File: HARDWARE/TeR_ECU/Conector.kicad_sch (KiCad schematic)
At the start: 1 part, among them IC1 MX34040NF2

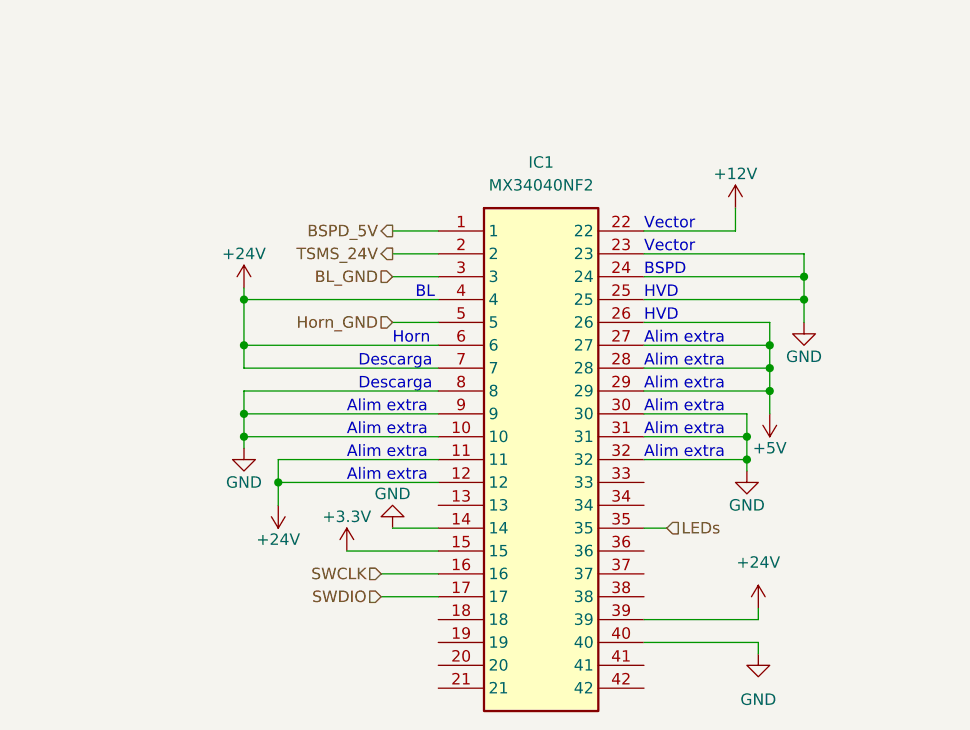
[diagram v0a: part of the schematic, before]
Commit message: Falata routear señales al conector
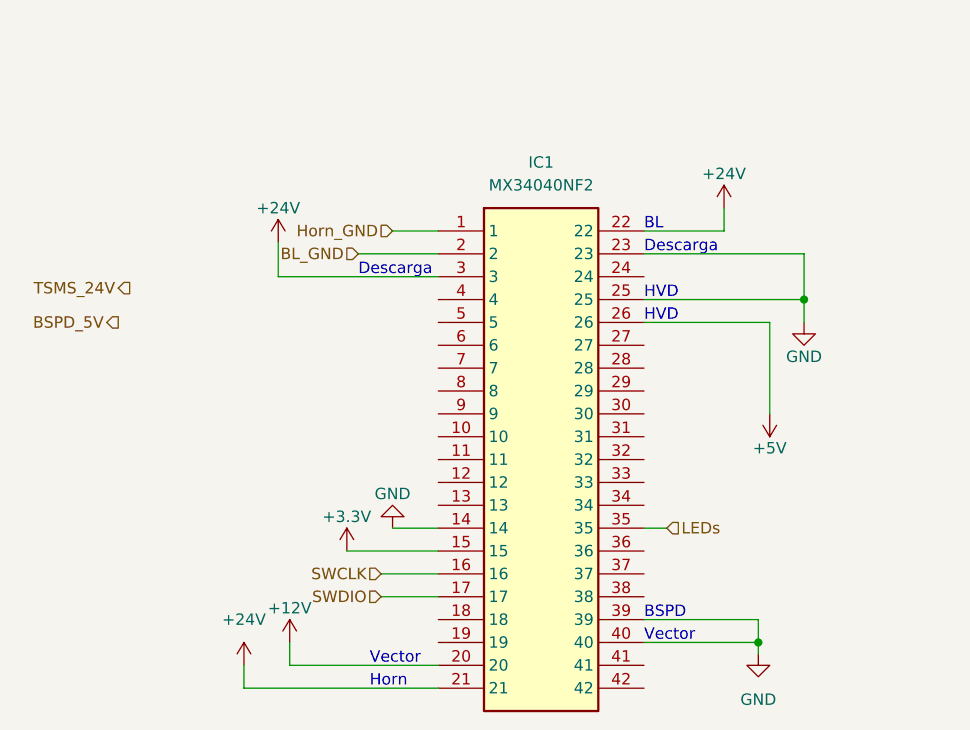
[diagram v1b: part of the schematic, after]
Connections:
- net +12V: now also IC1.20; no longer IC1.22
- net +24V: now also IC1.21, IC1.22, IC1.3; no longer IC1.11, IC1.12, IC1.39, IC1.4, IC1.6, IC1.7
- net +5V: no longer IC1.27, IC1.28, IC1.29
- net BL_GND: now also IC1.2; no longer IC1.3
- net BSPD_5V: no longer IC1.1
- net GND: now also IC1.39; no longer IC1.10, IC1.24, IC1.30, IC1.31, IC1.32, IC1.8, IC1.9
- net Horn_GND: now also IC1.1; no longer IC1.5
- net TSMS_24V: no longer IC1.2
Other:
- note removed: "Alim extra"

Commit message: Solo falta revisar
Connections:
- net +24V: now also IC1.8, IC1.9
- net +3.3V: now also IC1.5; no longer IC1.15
- net +5V: now also IC1.13, IC1.14, IC1.15, IC1.19, IC1.27; no longer IC1.26
- net BSPD_5V: now also IC1.17
- net GND: now also IC1.26, IC1.28, IC1.29, IC1.35, IC1.36, IC1.37, IC1.38; no longer IC1.14
- net LEDs: now also IC1.18; no longer IC1.35
- net SWCLK: now also IC1.4; no longer IC1.16
- net SWDIO: now also IC1.24; no longer IC1.17
- net TSMS_24V: now also IC1.16
- net UART_RX: now reaches IC1.6
- net UART_TX: now reaches IC1.7
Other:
- note added: "Extra 24V"
- note added: "Extra 5V"
- note added: "IMU"

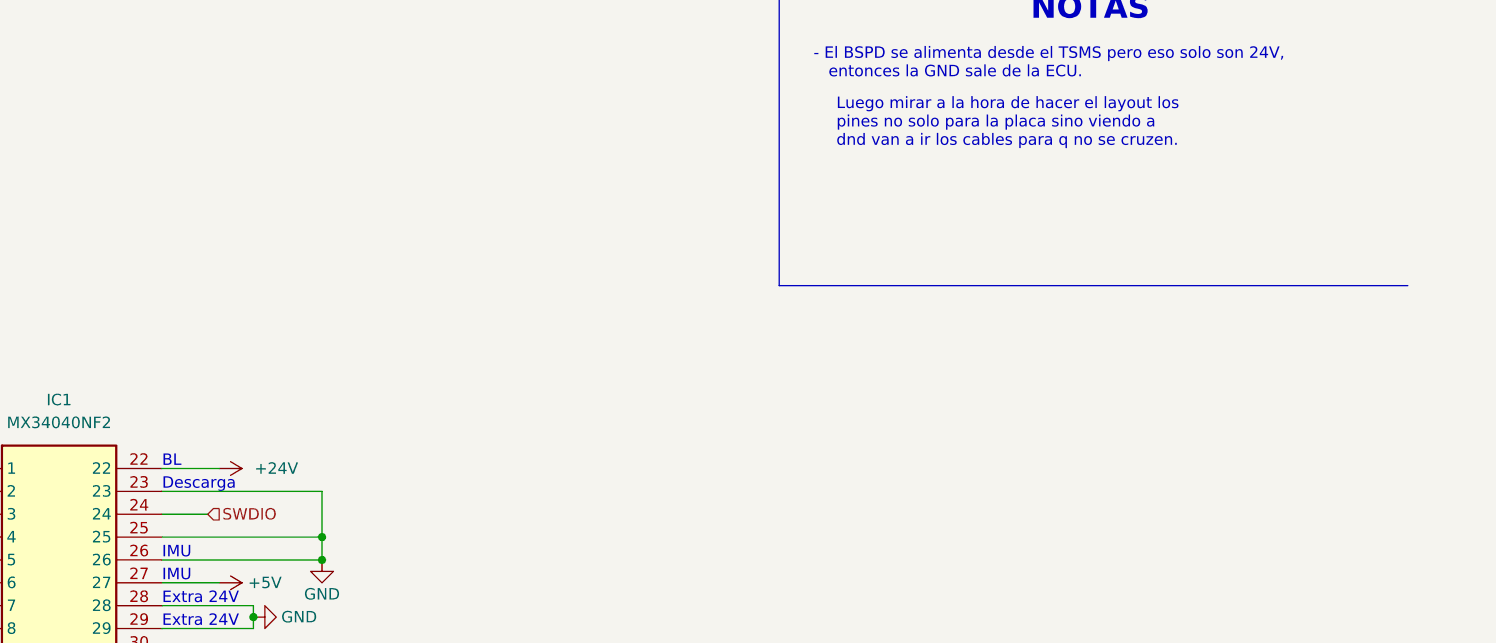
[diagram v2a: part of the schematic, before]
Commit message: Añadida resistencia luz de freno
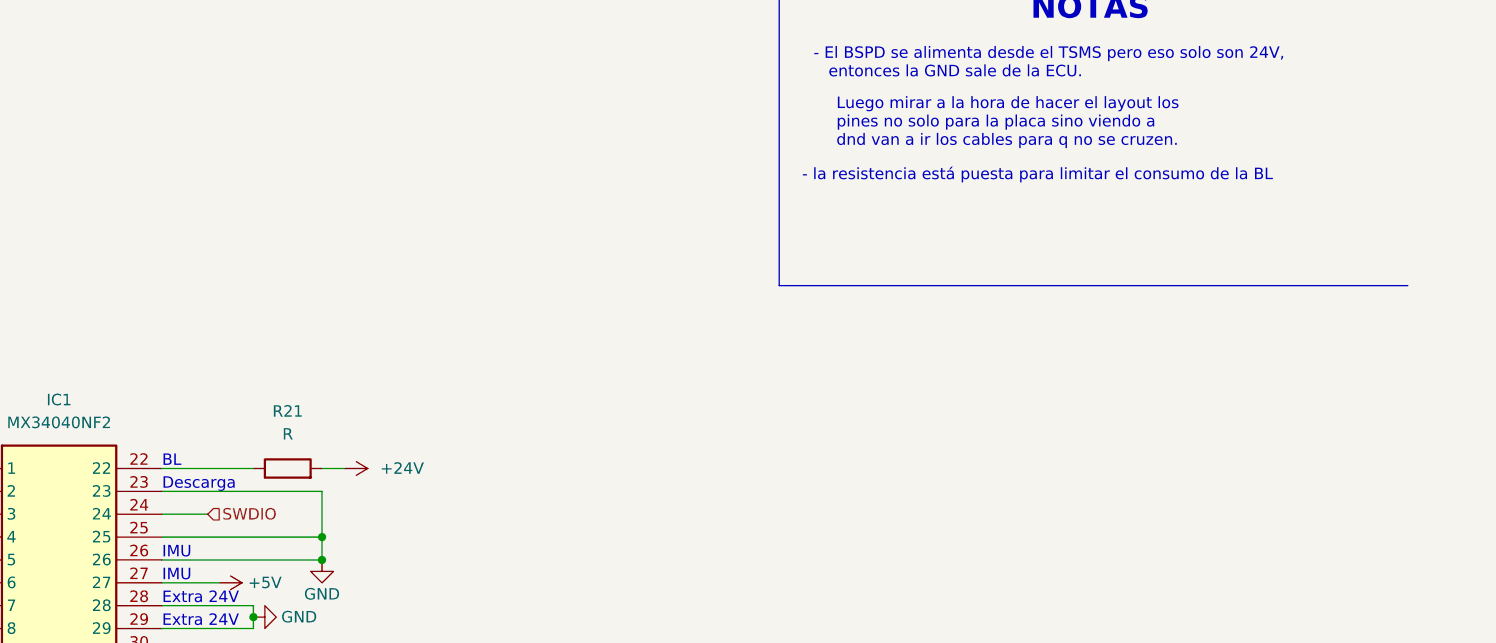
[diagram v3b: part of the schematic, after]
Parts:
- added R21: R, Resistor_SMD:R_0805_2012Metric, symbol Device:R
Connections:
- net +24V: now also R21.2; no longer IC1.22
- new net: IC1.22, R21.1
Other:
- note added: "- la resistencia está puesta para limitar el consumo de la BL"
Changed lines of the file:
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@@
     (stroke (width 0) (type default))
   )
-  (wire (pts (xy 147.32 68.58) (xy 153.67 68.58))
+  (wire (pts (xy 147.32 68.58) (xy 157.48 68.58))
     (stroke (width 0) (type default))
   )
@@
     (stroke (width 0) (type default))
   )
+  (wire (pts (xy 165.1 68.58) (xy 167.64 68.58))
+    (stroke (width 0) (type default))
+  )
   (wire (pts (xy 147.32 111.76) (xy 160.02 111.76))
     (stroke (width 0) (type default))
@@
   )
   (text "Descarga" (at 115.57 73.66 0)
+    (effects (font (size 1.27 1.27)) (justify left bottom))
+  )
+  (text "- la resistencia está puesta para limitar el consumo de la BL"
+    (at 218.44 36.83 0)
     (effects (font (size 1.27 1.27)) (justify left bottom))
   )
@@
         (path "/84413845-c4f3-4743-bcd2-a67649c90902/e25d0f8a-65a3-47e2-987f-518da8891580"
           (reference "#PWR065") (unit 1)
+        )
+      )
+    )
+  )
+  (symbol (lib_id "Device:R") (at 161.29 68.58 90) (unit 1)
+    (in_bom yes) (on_board yes) (dnp no) (fields_autoplaced)
+    (property "Reference" "R21" (at 161.29 62.23 90)
+      (effects (font (size 1.27 1.27)))
+    )
+    (property "Value" "R" (at 161.29 64.77 90)
+      (effects (font (size 1.27 1.27)))
+    )
+    (property "Footprint" "Resistor_SMD:R_0805_2012Metric" (at 161.29 70.358 90)
+      (effects (font (size 1.27 1.27)) hide)
+    )
+    (property "Datasheet" "~" (at 161.29 68.58 0)
+      (effects (font (size 1.27 1.27)) hide)
+    )
+    (pin "1")
+    (pin "2")
+    (instances
+      (project "TeR_ECU"
+        (path "/84413845-c4f3-4743-bcd2-a67649c90902/e25d0f8a-65a3-47e2-987f-518da8891580"
+          (reference "R21") (unit 1)
         )
       )
@@
     )
   )
-  (symbol (lib_id "power:+24V") (at 153.67 68.58 270) (unit 1)
-    (in_bom yes) (on_board yes) (dnp no)
-    (property "Reference" "#PWR067" (at 149.86 68.58 0)
-      (effects (font (size 1.27 1.27)) hide)
-    )
-    (property "Value" "+24V" (at 160.02 68.58 90)
-      (effects (font (size 1.27 1.27)))
-    )
-    (property "Footprint" "" (at 153.67 68.58 0)
-      (effects (font (size 1.27 1.27)) hide)
-    )
-    (property "Datasheet" "" (at 153.67 68.58 0)
-      (effects (font (size 1.27 1.27)) hide)
-    )
+  (symbol (lib_id "power:+24V") (at 167.64 68.58 270) (unit 1)
+    (in_bom yes) (on_board yes) (dnp no)
+    (property "Reference" "#PWR067" (at 163.83 68.58 0)
+      (effects (font (size 1.27 1.27)) hide)
+    )
+    (property "Value" "+24V" (at 173.99 68.58 90)
+      (effects (font (size 1.27 1.27)))
+    )
+    (property "Footprint" "" (at 167.64 68.58 0)
+      (effects (font (size 1.27 1.27)) hide)
+    )
+    (property "Datasheet" "" (at 167.64 68.58 0)
+      (effects (font (size 1.27 1.27)) hide)
+    )

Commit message: Rethought layout and footprints and fixed fuse normative problem
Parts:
- IC1: footprint MX34040NF2 -> MX34040NF2:MX34040NF2

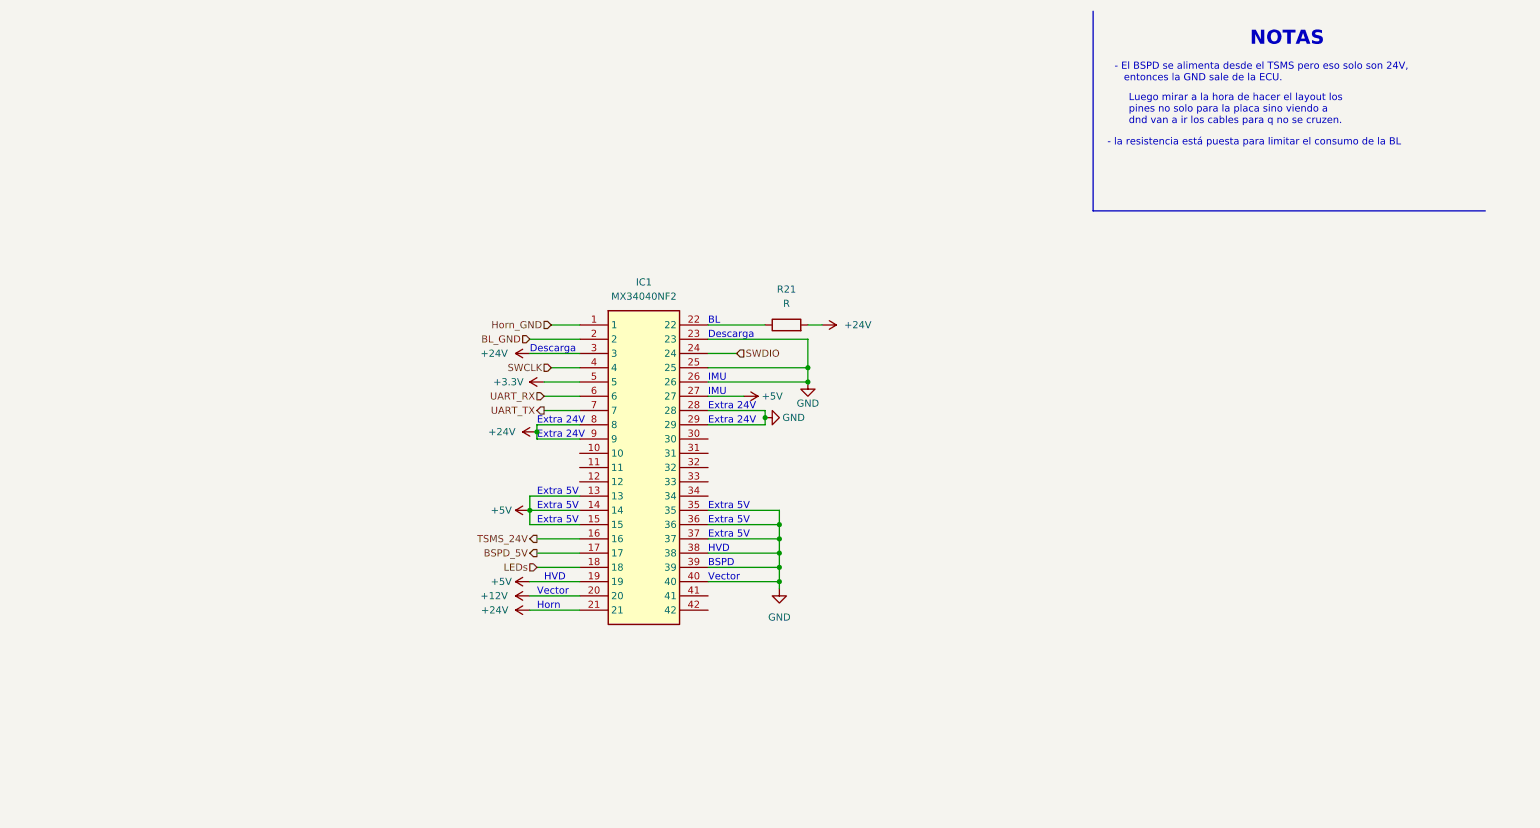
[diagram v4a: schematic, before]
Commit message: Layout V2, added 7-segment display, optimal placement of pins + rework of the boot headers(just one needed)
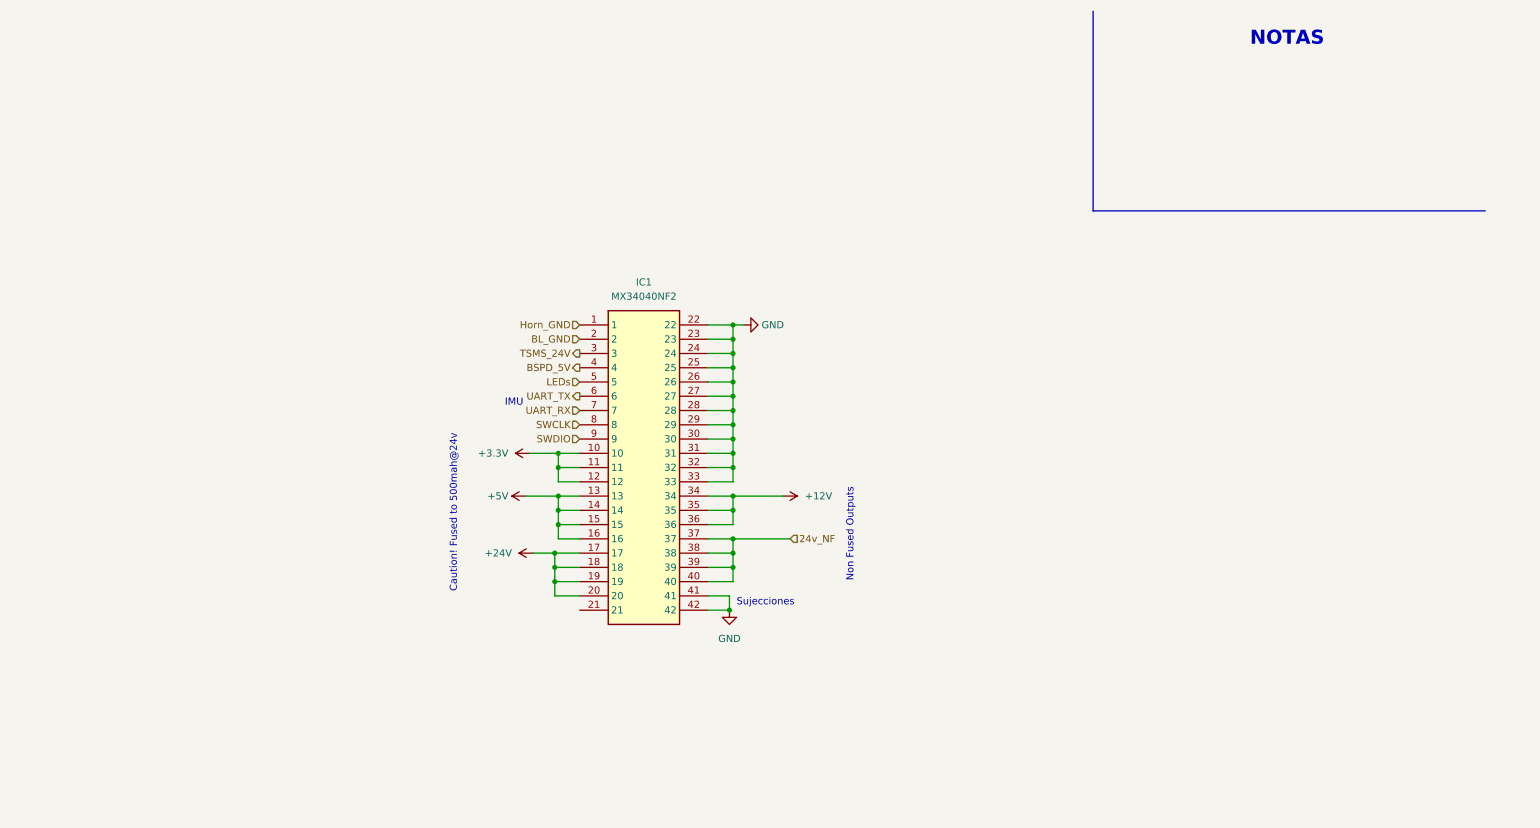
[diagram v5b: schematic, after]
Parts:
- removed R21: R, Resistor_SMD:R_0805_2012Metric, symbol Device:R
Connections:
- net +12V: now also IC1.34, IC1.35, IC1.36; no longer IC1.20
- net +24V: now also IC1.17, IC1.18, IC1.19, IC1.20; no longer IC1.21, IC1.3, IC1.8, IC1.9
- net +3.3V: now also IC1.10, IC1.11, IC1.12; no longer IC1.5
- net +5V: now also IC1.16; no longer IC1.19, IC1.27
- net BSPD_5V: now also IC1.4; no longer IC1.17
- net GND: now also IC1.22, IC1.24, IC1.27, IC1.30, IC1.31, IC1.32, IC1.33, IC1.41, IC1.42; no longer IC1.35, IC1.36, IC1.37, IC1.38, IC1.39, IC1.40
- net LEDs: now also IC1.5; no longer IC1.18
- net SWCLK: now also IC1.8; no longer IC1.4
- net SWDIO: now also IC1.9; no longer IC1.24
- net TSMS_24V: now also IC1.3; no longer IC1.16
- net UART_RX: now also IC1.7; no longer IC1.6
- net UART_TX: now also IC1.6; no longer IC1.7
- new net 24v_NF: IC1.37, IC1.38, IC1.39, IC1.40
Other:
- note added: "Caution! Fused to 500mah@24v"
- note added: "Non Fused Outputs"
- note added: "Sujecciones"
- note removed: "- El BSPD se alimenta desde el TSMS pero eso solo son 24V, entonces la GND sale de la ECU."
- note removed: "- la resistencia está puesta para limitar el consumo de la BL"
- note removed: "BL"
- note removed: "BSPD"
- note removed: "Descarga"
- note removed: "Extra 24V"
- note removed: "Extra 5V"
- note removed: "HVD"
- note removed: "Horn"
- note removed: "Luego mirar a la hora de hacer el layout los pines no solo para la placa sino viendo a dnd van a ir los cables para q no se cruzen."
- note removed: "Vector"

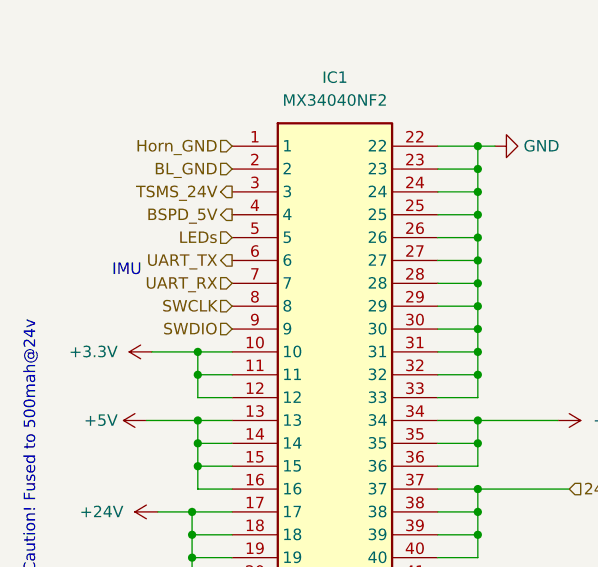
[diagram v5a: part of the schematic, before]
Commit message: Removed unnecesary via, DRC:Passes
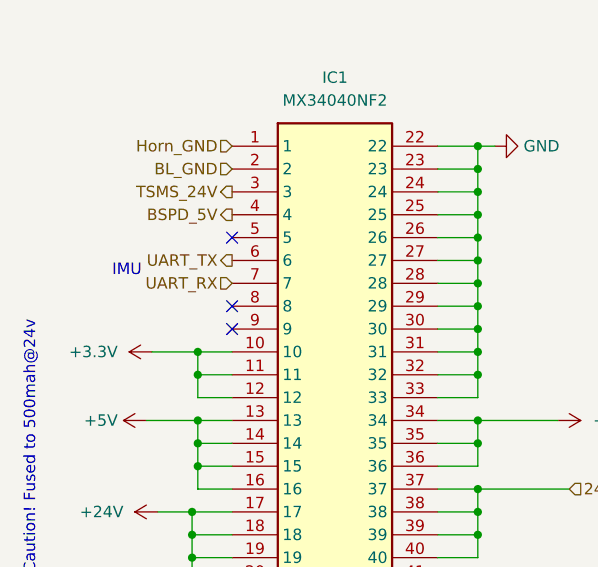
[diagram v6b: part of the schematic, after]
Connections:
- net LEDs: no longer names the net of IC1.5
- net SWCLK: no longer names the net of IC1.8
- net SWDIO: no longer names the net of IC1.9
- no-connect marks 0 -> 3
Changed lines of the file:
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@@
   (junction (at 151.765 88.9) (diameter 0) (color 0 0 0 0)
   )
+  (no_connect (at 124.46 86.36))
+  (no_connect (at 124.46 78.74))
+  (no_connect (at 124.46 88.9))
   (wire (pts (xy 151.765 106.68) (xy 151.765 109.22))
     (stroke (width 0) (type default))
@@
     (effects (font (size 1.27 1.27)) (justify right))
   )
-  (hierarchical_label "SWDIO" (shape input) (at 124.46 88.9 180) (fields_autoplaced)
-    (effects (font (size 1.27 1.27)) (justify right))
-  )
   (hierarchical_label "24v_NF" (shape input) (at 161.925 106.68 0) (fields_autoplaced)
     (effects (font (size 1.27 1.27)) (justify left))
@@
     (effects (font (size 1.27 1.27)) (justify right))
   )
-  (hierarchical_label "SWCLK" (shape input) (at 124.46 86.36 180) (fields_autoplaced)
-    (effects (font (size 1.27 1.27)) (justify right))
-  )
-  (hierarchical_label "LEDs" (shape input) (at 124.46 78.74 180) (fields_autoplaced)
-    (effects (font (size 1.27 1.27)) (justify right))
-  )
